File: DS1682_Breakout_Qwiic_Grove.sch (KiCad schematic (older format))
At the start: 12 parts, among them J1 2p-smd-1.0-90d, J2 H4P-SMD-2.0, U2 BSS138PS, U3 XC6206MR

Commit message: Add part and update iBOM
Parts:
- C1, C2: manf# (none) -> C0603C105K8PAC7411
- C3: manf# (none) -> C0603C104K8RACTU
- D1: manf# (none) -> DS1683S+T&R
- H1: manf# (none) -> LTST-C190KRKT
- J1: manf# (none) -> SM02B-SRSS-TB(LF)(SN)
- J2: manf# (none) -> 114020163
- R1: manf# (none) -> CR0603-FX-5110ELF
- R2: manf# (none) -> CRT0805-FZ-1002ELF
- R7: manf# (none) -> CAY16-103J4LF
- U2: manf# (none) -> BSS138PS,115
- U3: manf# (none) -> MCP1811AT-033/TT
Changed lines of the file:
@@
 F 2 "DS1682_Breakout_Qwiic_Grove:SOT23" H 4200 1200 50  0001 C CNN
 F 3 "" H 4200 1200 50  0001 C CNN
+F 4 "MCP1811AT-033/TT" H 4200 1200 50  0001 C CNN "manf#"
 	1    4200 1200
 	1    0    0    -1
@@
 F 2 "DS1682_Breakout_Qwiic_Grove:C0603" H 3600 1600 50  0001 C CNN
 F 3 "" H 3600 1600 50  0001 C CNN
+F 4 "C0603C105K8PAC7411" H 3600 1600 50  0001 C CNN "manf#"
 	1    3600 1600
 	0    -1   -1   0
@@
 F 2 "DS1682_Breakout_Qwiic_Grove:C0603" H 4750 1600 50  0001 C CNN
 F 3 "" H 4750 1600 50  0001 C CNN
+F 4 "C0603C105K8PAC7411" H 4750 1600 50  0001 C CNN "manf#"
 	1    4750 1600
 	0    -1   -1   0
@@
 F 2 "DS1682_Breakout_Qwiic_Grove:C0603" H 4950 1600 50  0001 C CNN
 F 3 "" H 4950 1600 50  0001 C CNN
+F 4 "C0603C104K8RACTU" H 4950 1600 50  0001 C CNN "manf#"
 	1    4950 1600
 	0    -1   -1   0
@@
 F 2 "DS1682_Breakout_Qwiic_Grove:HW4-SMD-2.0" H 5900 2400 50  0001 C CNN
 F 3 "" H 5900 2400 50  0001 C CNN
+F 4 "114020163" H 5900 2400 50  0001 C CNN "manf#"
 	1    5900 2400
 	1    0    0    -1
@@
 F 2 "DS1682_Breakout_Qwiic_Grove:SOT65P210X110-6N" H 3700 2700 50  0001 C CNN
 F 3 "" H 3700 2700 50  0001 C CNN
+F 4 "BSS138PS,115" H 3700 2700 50  0001 C CNN "manf#"
 	1    3700 2700
 	1    0    0    -1
@@
 F 2 "DS1682_Breakout_Qwiic_Grove:1206-8-3.3X2.4" H 2700 2600 50  0001 C CNN
 F 3 "" H 2700 2600 50  0001 C CNN
+F 4 "CAY16-103J4LF" H 2700 2600 50  0001 C CNN "manf#"
 	1    2700 2600
 	1    0    0    -1
@@
 F 2 "DS1682_Breakout_Qwiic_Grove:1206-8-3.3X2.4" H 2700 2700 50  0001 C CNN
 F 3 "" H 2700 2700 50  0001 C CNN
+F 4 "CAY16-103J4LF" H 2700 2700 50  0001 C CNN "manf#"
 	2    2700 2700
 	1    0    0    -1
@@
 F 2 "DS1682_Breakout_Qwiic_Grove:1206-8-3.3X2.4" H 4600 2600 50  0001 C CNN
 F 3 "" H 4600 2600 50  0001 C CNN
+F 4 "CAY16-103J4LF" H 4600 2600 50  0001 C CNN "manf#"
 	3    4600 2600
 	1    0    0    -1
@@
 F 2 "DS1682_Breakout_Qwiic_Grove:1206-8-3.3X2.4" H 4600 2700 50  0001 C CNN
 F 3 "" H 4600 2700 50  0001 C CNN
+F 4 "CAY16-103J4LF" H 4600 2700 50  0001 C CNN "manf#"
 	4    4600 2700
 	1    0    0    -1
@@
 F 2 "DS1682_Breakout_Qwiic_Grove:SOIC8-N_MC" H 7900 3000 50  0001 C CNN
 F 3 "" H 7900 3000 50  0001 C CNN
+F 4 "DS1683S+T&R" H 7900 3000 50  0001 C CNN "manf#"
 	1    7900 3000
 	1    0    0    -1
@@
 F 2 "DS1682_Breakout_Qwiic_Grove:R0603" H 6500 3000 50  0001 C CNN
 F 3 "" H 6500 3000 50  0001 C CNN
+F 4 "CR0603-FX-5110ELF" H 6500 3000 50  0001 C CNN "manf#"
 	1    6500 3000
 	-1   0    0    1
@@
 F 2 "DS1682_Breakout_Qwiic_Grove:CHIPLED_0603" H 6900 3000 50  0001 C CNN
 F 3 "" H 6900 3000 50  0001 C CNN
+F 4 "LTST-C190KRKT" H 6900 3000 50  0001 C CNN "manf#"
 	1    6900 3000
 	0    -1   1    0
@@
 F 2 "DS1682_Breakout_Qwiic_Grove:R0603" H 7000 2400 50  0001 C CNN
 F 3 "" H 7000 2400 50  0001 C CNN
+F 4 "CRT0805-FZ-1002ELF" H 7000 2400 50  0001 C CNN "manf#"
 	1    7000 2400
 	0    1    1    0
@@
 F 2 "DS1682_Breakout_Qwiic_Grove:HW2-SMD-1.0-90D" H 8000 1000 50  0001 C CNN
 F 3 "" H 8000 1000 50  0001 C CNN
+F 4 "SM02B-SRSS-TB(LF)(SN)" H 8000 1000 50  0001 C CNN "manf#"
 	1    8000 1000
 	-1   0    0    1

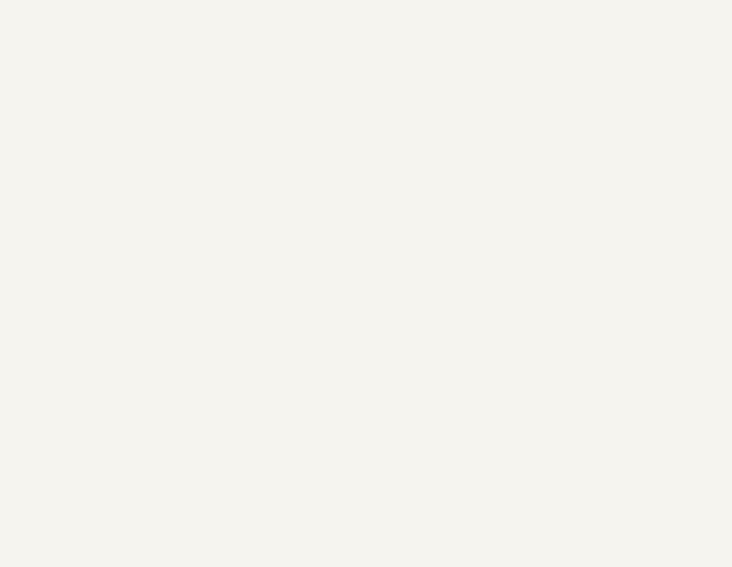
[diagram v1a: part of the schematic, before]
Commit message: Add LOGO1 alternative
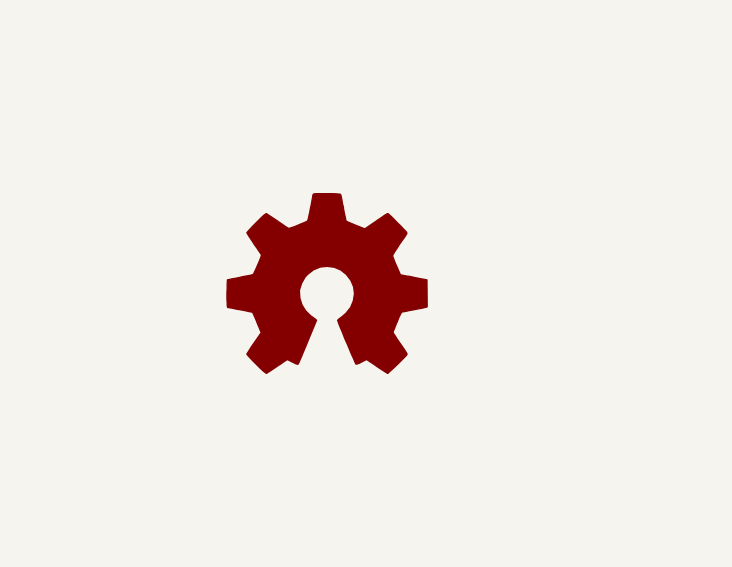
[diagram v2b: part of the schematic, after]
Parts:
- added LOGO1: Logo_Open_Hardware_Large, DS1682_Breakout_Qwiic_Grove:OSHW_FILLX200_NOTEXT, symbol Graphic:Logo_Open_Hardware_Large
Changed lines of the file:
@@
 Text Notes 4050 2000 0    59   ~ 0
 稳压电路
+$Comp
+L Graphic:Logo_Open_Hardware_Large LOGO1
+U 1 1 5F9E751C
+P 3584 5278
+F 0 "LOGO1" H 3584 5778 50  0001 C CNN
+F 1 "Logo_Open_Hardware_Large" H 3584 4878 50  0001 C CNN
+F 2 "DS1682_Breakout_Qwiic_Grove:OSHW_FILLX200_NOTEXT" H 3584 5278 50  0001 C CNN
+F 3 "~" H 3584 5278 50  0001 C CNN
+	1    3584 5278
+	1    0    0    -1
+$EndComp
 $EndSCHEMATC
